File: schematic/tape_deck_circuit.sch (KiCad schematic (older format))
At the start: 22 parts

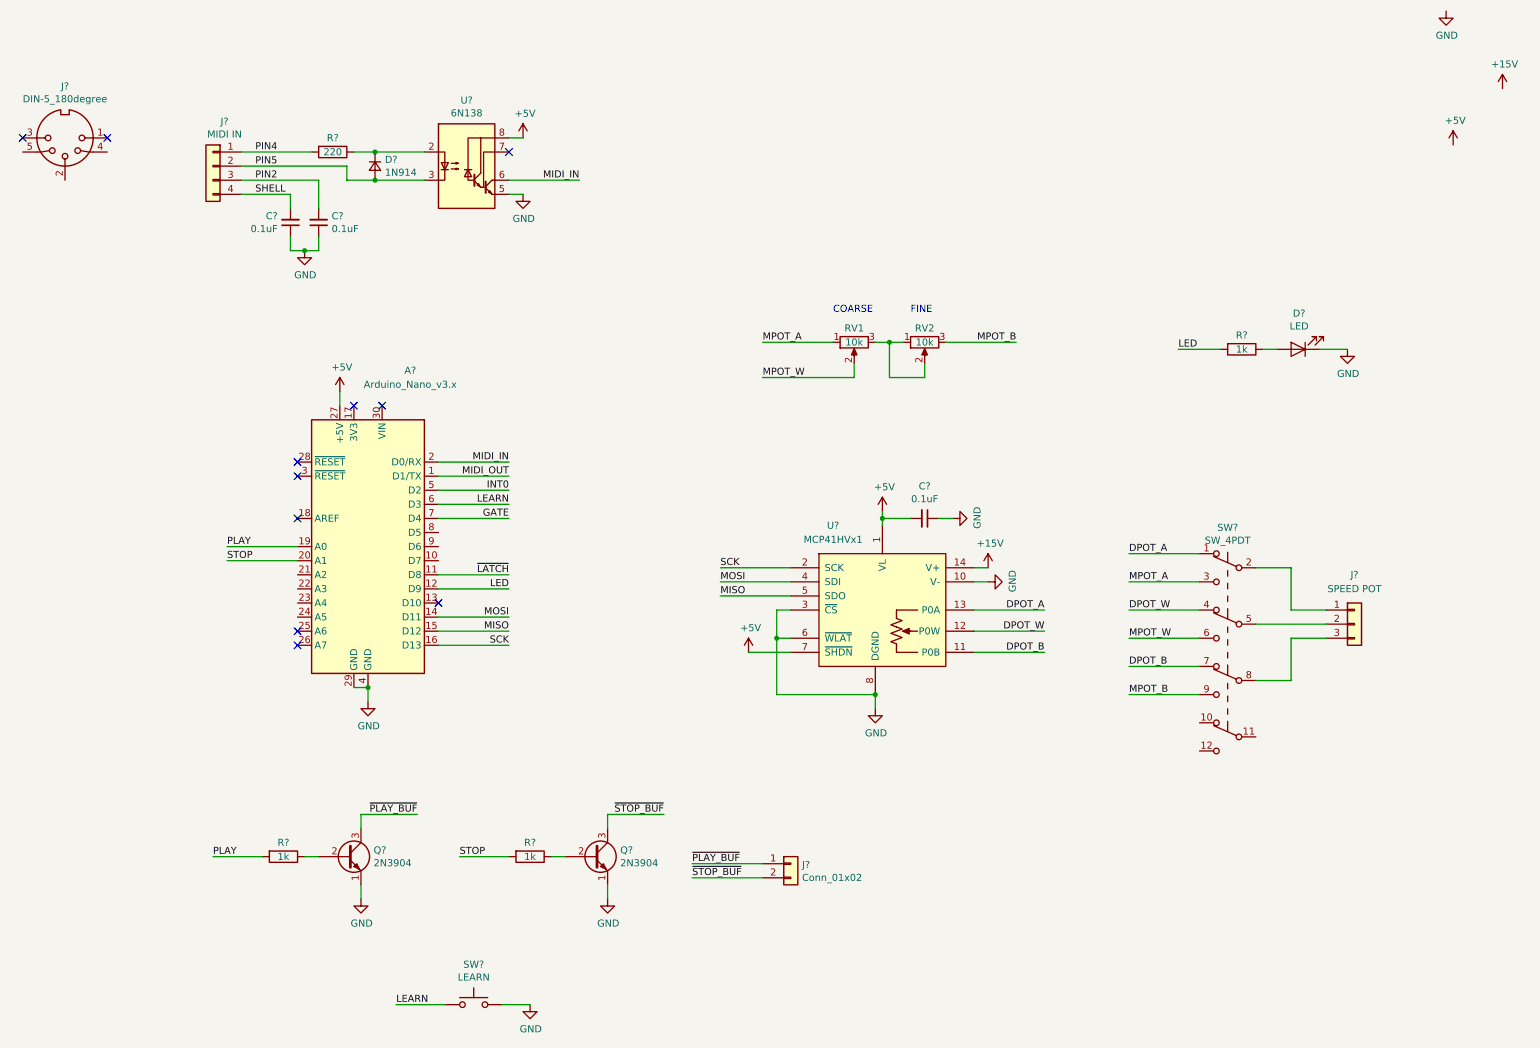
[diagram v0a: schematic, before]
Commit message: Add results from experiments with 2 digital pots
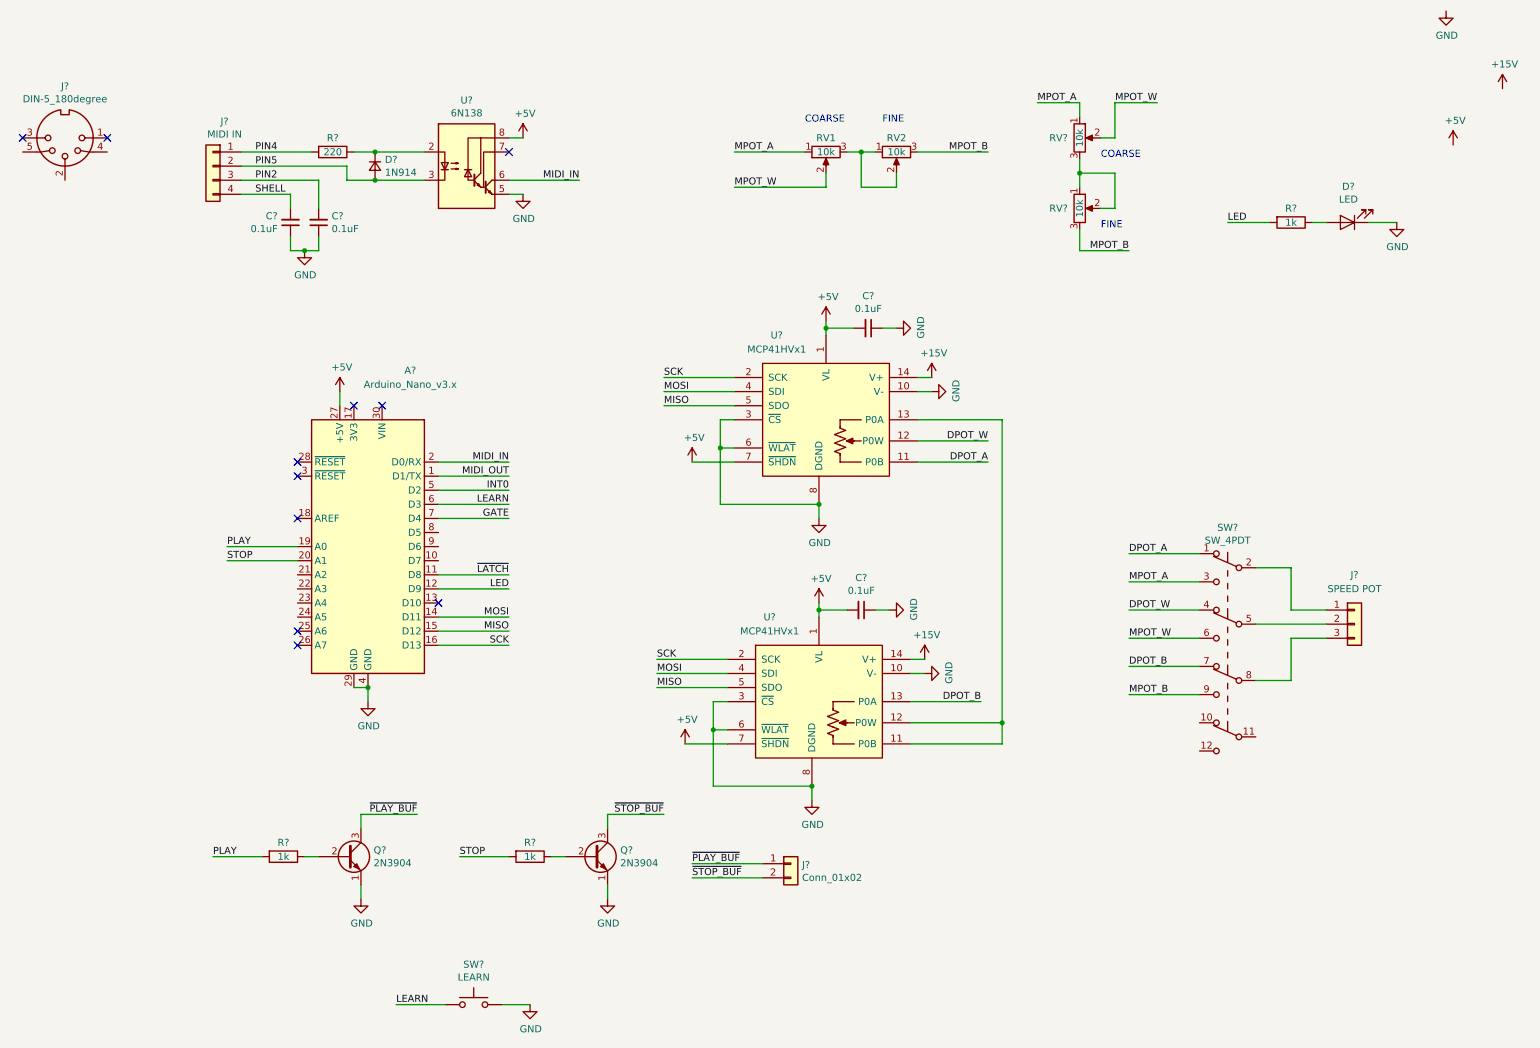
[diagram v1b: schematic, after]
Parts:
- added C?: 0.1uF, symbol Device:C_Small
- added RV? (x2): 10k, symbol Device:R_POT
- added U?: MCP41HVx1, symbol midi_tape_deck:MCP41HVx1
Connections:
- net +15V: now also U?.14 (V+)
- net +5V: now also C?.2, U?.1 (VL), U?.7 (~SHDN)
- net DPOT_A: now also U?.11 (P0B); no longer U?.13 (P0A)
- net DPOT_B: now also U?.13 (P0A); no longer U?.11 (P0B)
- net GND: now also C?.1, U?.10 (V-), U?.3 (~CS), U?.6 (~WLAT), U?.8 (DGND), U?.9 (NC)
- net MISO: now also U?.5 (SDO)
- net MOSI: now also U?.4 (SDI)
- net MPOT_A: now also RV?.1
- net MPOT_B: now also RV?.3
- net MPOT_W: now also RV?.2
- net SCK: now also U?.2 (SCK)
- new net: U?.11 (P0B), U?.12 (P0W), U?.13 (P0A)
- new net: RV?.1, RV?.2, RV?.3
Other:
- moved on the sheet: C?, D?, R?, RV1, RV2, U?

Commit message: Start working out protoboard layout
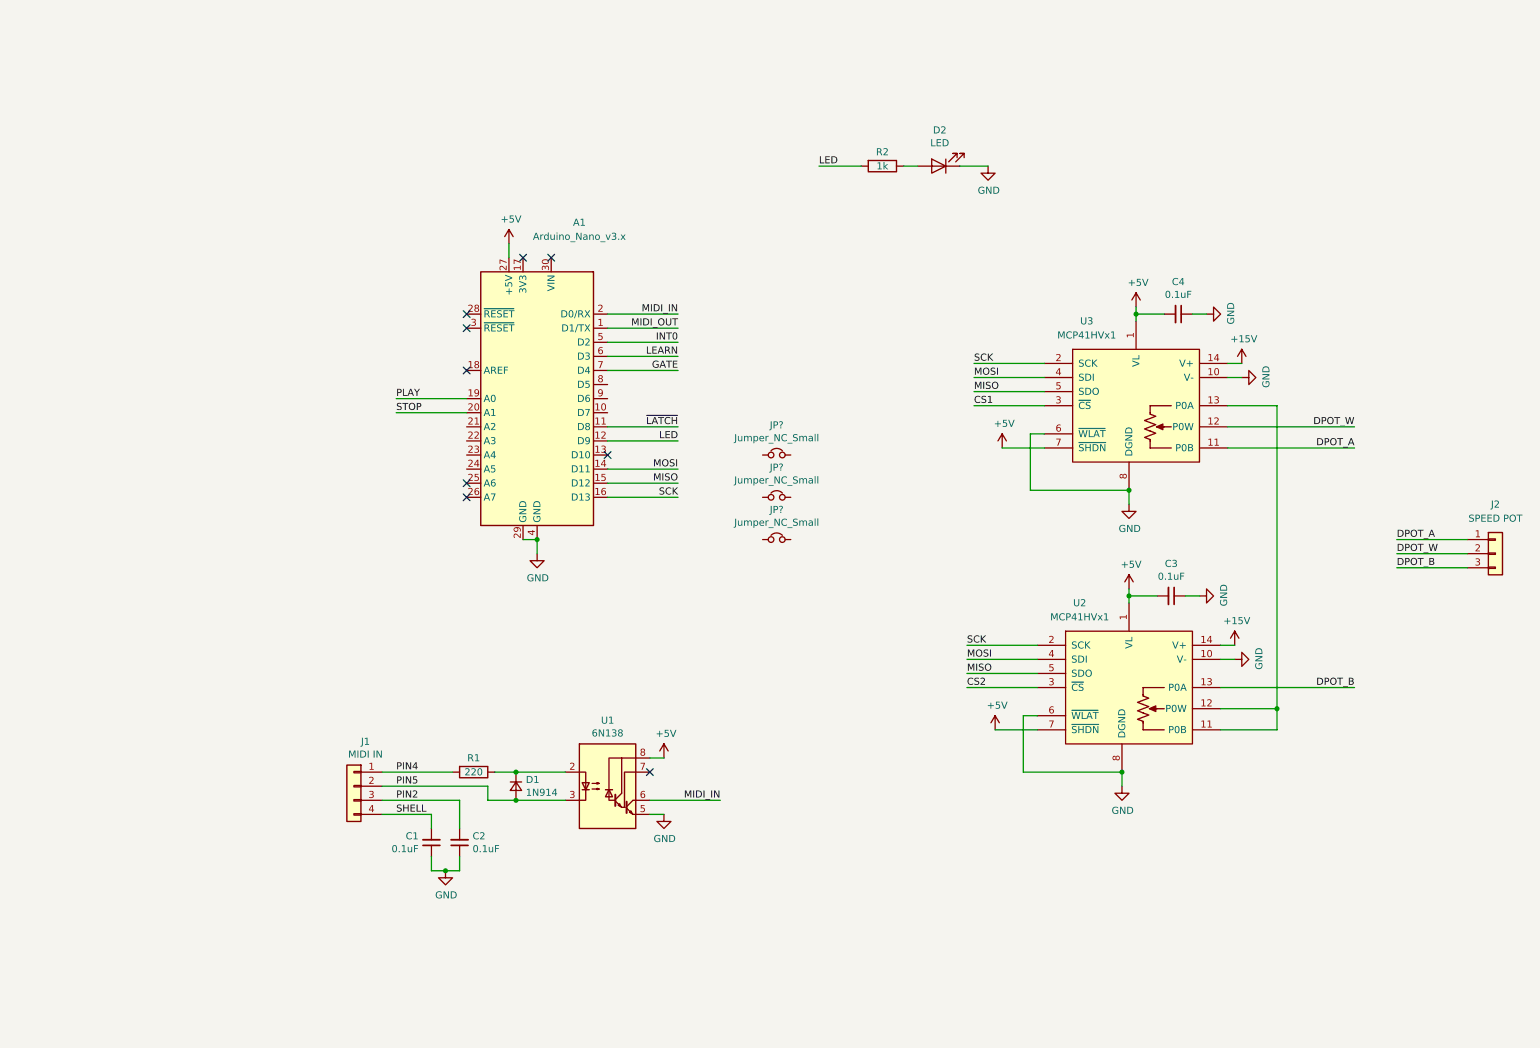
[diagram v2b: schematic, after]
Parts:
- removed J?: DIN-5_180degree, symbol Connector:DIN-5_180degree
- removed J?: Conn_01x02, symbol Connector_Generic:Conn_01x02
- removed Q? (x2): 2N3904, symbol Device:Q_NPN_EBC
- removed R? (x2): 1k, symbol Device:R
- removed RV1, RV2, RV? (x2): 10k, symbol Device:R_POT
- removed SW?: SW_4PDT, symbol midi_tape_deck:SW_4PDT
- removed SW?: LEARN, symbol Switch:SW_Push
- added JP? (x3): Jumper_NC_Small, symbol Device:Jumper_NC_Small
- C1, C2, C3, C4: renamed from C?; footprint (none) -> Capacitors_THT:C_Disc_D3.0mm_W1.6mm_P2.50mm
- D1: renamed from D?; footprint (none) -> Diodes_THT:D_DO-35_SOD27_P7.62mm_Horizontal
- D2: renamed from D?; footprint (none) -> Pin_Headers:Pin_Header_Straight_1x02_Pitch2.54mm
- J1: renamed from J?; footprint (none) -> Pin_Headers:Pin_Header_Straight_1x04_Pitch2.54mm
- J2: renamed from J?; footprint (none) -> Pin_Headers:Pin_Header_Straight_1x03_Pitch2.54mm
- R1, R2: renamed from R?; footprint (none) -> Resistors_THT:R_Axial_DIN0207_L6.3mm_D2.5mm_P10.16mm_Horizontal
- U1: renamed from U?; footprint (none) -> Housings_DIP:DIP-8_W7.62mm_Socket
- gave numbers to parts that had none: 3
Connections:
- net DPOT_A: now also J2.1 (Pin_1)
- net DPOT_B: now also J2.3 (Pin_3)
- net DPOT_W: now also J2.2 (Pin_2)
- net GND: no longer U2.3 (~CS), U3.3 (~CS)
- new net CS1: U3.3 (~CS)
- new net CS2: U2.3 (~CS)
- no-connect marks 11 -> 9
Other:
- note removed: "COARSE"
- note removed: "FINE"
- moved on the sheet: A1, C1, C2, C3, C4, D1, D2, J1, J2, R1, R2, U1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

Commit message: Continue protoboard layout
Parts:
- removed JP? (x3): Jumper_NC_Small, symbol Device:Jumper_NC_Small
- added J3: POWER, Connector_PinHeader_2.54mm:PinHeader_1x03_P2.54mm_Vertical, symbol Connector_Generic:Conn_01x03
- D2: footprint Pin_Headers:Pin_Header_Straight_1x02_Pitch2.54mm -> Connector_PinHeader_2.54mm:PinHeader_1x02_P2.54mm_Vertical
- J1: footprint Pin_Headers:Pin_Header_Straight_1x04_Pitch2.54mm -> Connector_PinHeader_2.54mm:PinHeader_1x04_P2.54mm_Vertical
- J2: footprint Pin_Headers:Pin_Header_Straight_1x03_Pitch2.54mm -> Connector_PinHeader_2.54mm:PinHeader_1x03_P2.54mm_Vertical
- U2: renamed from U3; footprint (none) -> midi_tape_deck:TSSOP_Breakout
- U3: renamed from U2; footprint (none) -> midi_tape_deck:TSSOP_Breakout
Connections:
- net INT0 is gone; now on net LEARN: A1.5 (D2)
- net PLAY is gone; now on net GATE: A1.19 (A0)
- net +15V: now also J3.3 (Pin_3)
- net +5V: now also J3.1 (Pin_1)
- net CS1: now also A1.23 (A4)
- net CS2: now also A1.24 (A5)
- net GATE: no longer A1.7 (D4)
- net GND: now also J3.2 (Pin_2)
- net LEARN: no longer A1.6 (D3)
- net LED: now also A1.9 (D6); no longer A1.12 (D9)
- net POT_COM: now reaches U2.13 (P0A), U3.11 (P0B), U3.12 (P0W)
- net STOP: no longer names the net of A1.20 (A1)
- net ~LATCH: no longer names the net of A1.11 (D8)
- new net INT1: A1.6 (D3)
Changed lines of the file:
@@
 EESchema Schematic File Version 4
+LIBS:tape_deck_circuit-cache
 EELAYER 30 0
 EELAYER END
@@
 $EndComp
 $Comp
-L midi_tape_deck:MCP41HVx1 U3
+L midi_tape_deck:MCP41HVx1 U2
 U 1 1 6108BB45
 P 7650 3000
-F 0 "U3" H 7300 3650 50  0000 C CNN
+F 0 "U2" H 7300 3650 50  0000 C CNN
 F 1 "MCP41HVx1" H 7300 3550 50  0000 C CNN
-F 2 "" H 7450 3150 50  0001 C CNN
+F 2 "midi_tape_deck:TSSOP_Breakout" H 7450 3150 50  0001 C CNN
 F 3 "" H 7450 3150 50  0001 C CNN
 	1    7650 3000
@@
 MOSI
 Wire Wire Line
-	4400 3500 3900 3500
-Wire Wire Line
 	4400 3400 3900 3400
 $Comp
@@
 Wire Wire Line
 	7850 2300 7650 2300
+Text Label 4400 2600 2    50   ~ 0
+INT1
 Text Label 4400 2500 2    50   ~ 0
-INT0
-Text Label 4400 2600 2    50   ~ 0
 LEARN
 Wire Wire Line
@@
 	4400 2400 3900 2400
 NoConn ~ 3900 3300
-Text Label 4400 3100 2    50   ~ 0
-~LATCH
-Wire Wire Line
-	3900 3100 4400 3100
-Text Label 2400 2900 0    50   ~ 0
-PLAY
-Text Label 2400 3000 0    50   ~ 0
-STOP
+Wire Wire Line
+	2900 3300 2400 3300
 $Comp
 L Isolator:6N138 U1
@@
 F 0 "J1" H 2018 5967 50  0000 C CNN
 F 1 "MIDI IN" H 2018 5876 50  0000 C CNN
-F 2 "Pin_Headers:Pin_Header_Straight_1x04_Pitch2.54mm" H 2100 5650 50  0001 C CNN
+F 2 "Connector_PinHeader_2.54mm:PinHeader_1x04_P2.54mm_Vertical" H 2100 5650 50  0001 C CNN
 F 3 "~" H 2100 5650 50  0001 C CNN
 	1    2100 5650
@@
 Wire Wire Line
 	8300 3100 9200 3100
-Text Label 4400 3200 2    50   ~ 0
+Text Label 4400 2900 2    50   ~ 0
 LED
 Wire Wire Line
-	4400 3200 3900 3200
+	4400 2900 3900 2900
 $Comp
 L Device:LED D2
@@
 F 0 "D2" H 6243 995 50  0000 C CNN
 F 1 "LED" H 6243 1086 50  0000 C CNN
-F 2 "Pin_Headers:Pin_Header_Straight_1x02_Pitch2.54mm" H 6250 1250 50  0001 C CNN
+F 2 "Connector_PinHeader_2.54mm:PinHeader_1x02_P2.54mm_Vertical" H 6250 1250 50  0001 C CNN
 F 3 "~" H 6250 1250 50  0001 C CNN
 	1    6250 1250
@@
 Wire Wire Line
 	6600 1250 6400 1250
-Wire Wire Line
-	2400 2900 2900 2900
-Wire Wire Line
-	2900 3000 2400 3000
-Text Label 4400 2700 2    50   ~ 0
+Text Label 2400 2900 0    50   ~ 0
 GATE
 Wire Wire Line
-	3900 2700 4400 2700
+	2900 2900 2400 2900
 Wire Wire Line
 	7000 3150 6900 3150
@@
 SCK
 $Comp
-L midi_tape_deck:MCP41HVx1 U2
+L midi_tape_deck:MCP41HVx1 U3
 U 1 1 61291371
 P 7600 5000
-F 0 "U2" H 7250 5650 50  0000 C CNN
+F 0 "U3" H 7250 5650 50  0000 C CNN
 F 1 "MCP41HVx1" H 7250 5550 50  0000 C CNN
-F 2 "" H 7400 5150 50  0001 C CNN
+F 2 "midi_tape_deck:TSSOP_Breakout" H 7400 5150 50  0001 C CNN
 F 3 "" H 7400 5150 50  0001 C CNN
 	1    7600 5000
@@
 F 0 "J2" H 10200 4350 50  0000 C CNN
 F 1 "SPEED POT" H 10200 4250 50  0000 C CNN
-F 2 "Pin_Headers:Pin_Header_Straight_1x03_Pitch2.54mm" H 10200 4000 50  0001 C CNN
+F 2 "Connector_PinHeader_2.54mm:PinHeader_1x03_P2.54mm_Vertical" H 10200 4000 50  0001 C CNN
 F 3 "~" H 10200 4000 50  0001 C CNN
 	1    10200 4000
@@
 Wire Wire Line
 	9500 4000 10000 4000
-$Comp
-L Device:Jumper_NC_Small JP?
-U 1 1 61329052
-P 5100 3300
-F 0 "JP?" H 5100 3512 50  0000 C CNN
-F 1 "Jumper_NC_Small" H 5100 3421 50  0000 C CNN
-F 2 "" H 5100 3300 50  0001 C CNN
-F 3 "~" H 5100 3300 50  0001 C CNN
-	1    5100 3300
-	1    0    0    -1
-$EndComp
-$Comp
-L Device:Jumper_NC_Small JP?
-U 1 1 6132985B
-P 5100 3600
-F 0 "JP?" H 5100 3812 50  0000 C CNN
-F 1 "Jumper_NC_Small" H 5100 3721 50  0000 C CNN
-F 2 "" H 5100 3600 50  0001 C CNN
-F 3 "~" H 5100 3600 50  0001 C CNN
-	1    5100 3600
-	1    0    0    -1
-$EndComp
-$Comp
-L Device:Jumper_NC_Small JP?
-U 1 1 61329ACE
-P 5100 3900
-F 0 "JP?" H 5100 4112 50  0000 C CNN
-F 1 "Jumper_NC_Small" H 5100 4021 50  0000 C CNN
-F 2 "" H 5100 3900 50  0001 C CNN
-F 3 "~" H 5100 3900 50  0001 C CNN
-	1    5100 3900
-	1    0    0    -1
-$EndComp
 Connection ~ 7600 4300
 Wire Wire Line
@@
 Wire Wire Line
 	7650 2300 7650 2350
+Text Label 2400 3300 0    50   ~ 0
+CS1
+Text Label 2400 3400 0    50   ~ 0
+CS2
+Wire Wire Line
+	2400 3400 2900 3400
+Text Label 8300 5250 0    50   ~ 0
+POT_COM
+Wire Wire Line
+	4400 3500 3900 3500
+$Comp
+L Connector_Generic:Conn_01x03 J3
+U 1 1 6139A277
+P 1700 2000
+F 0 "J3" H 1700 2350 50  0000 C CNN
+F 1 "POWER" H 1700 2250 50  0000 C CNN
+F 2 "Connector_PinHeader_2.54mm:PinHeader_1x03_P2.54mm_Vertical" H 1700 2000 50  0001 C CNN
+F 3 "~" H 1700 2000 50  0001 C CNN
+	1    1700 2000
+	1    0    0    -1
+$EndComp
+$Comp
+L power:+5V #PWR0119
+U 1 1 6139C45A
+P 1000 1750
+F 0 "#PWR0119" H 1000 1600 50  0001 C CNN
+F 1 "+5V" H 1015 1923 50  0000 C CNN
+F 2 "" H 1000 1750 50  0001 C CNN
+F 3 "" H 1000 1750 50  0001 C CNN
+	1    1000 1750
+	1    0    0    -1
+$EndComp
+$Comp
+L power:+15V #PWR0120
+U 1 1 6139C6F8
+P 1000 2500
+F 0 "#PWR0120" H 1000 2350 50  0001 C CNN
+F 1 "+15V" H 1015 2673 50  0000 C CNN
+F 2 "" H 1000 2500 50  0001 C CNN
+F 3 "" H 1000 2500 50  0001 C CNN
+	1    1000 2500
+	1    0    0    -1
+$EndComp
+$Comp
+L power:GND #PWR0121
+U 1 1 6139D73C
+P 1000 2000
+F 0 "#PWR0121" H 1000 1750 50  0001 C CNN
+F 1 "GND" H 1005 1827 50  0000 C CNN
+F 2 "" H 1000 2000 50  0001 C CNN
+F 3 "" H 1000 2000 50  0001 C CNN
+	1    1000 2000
+	1    0    0    -1
+$EndComp
+Wire Wire Line
+	1000 2000 1500 2000
+Wire Wire Line
+	1000 1750 1000 1900
+Wire Wire Line
+	1000 1900 1500 1900
+Wire Wire Line
+	1500 2100 1500 2500
+Wire Wire Line
+	1500 2500 1000 2500
 $EndSCHEMATC
